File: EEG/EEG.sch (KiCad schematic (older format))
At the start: 45 parts, among them J1 USB_B_Micro, J2 Conn_01x08_Female, J3 Conn_01x08_Female, Q1 2N2219, Q2 2N2219, SW1 SW_Push, SW2 SW_Push, U1 AMS1117-3.3, U2 FT231XS, U3 ESP32-PICO-D4, U4 MAX7219

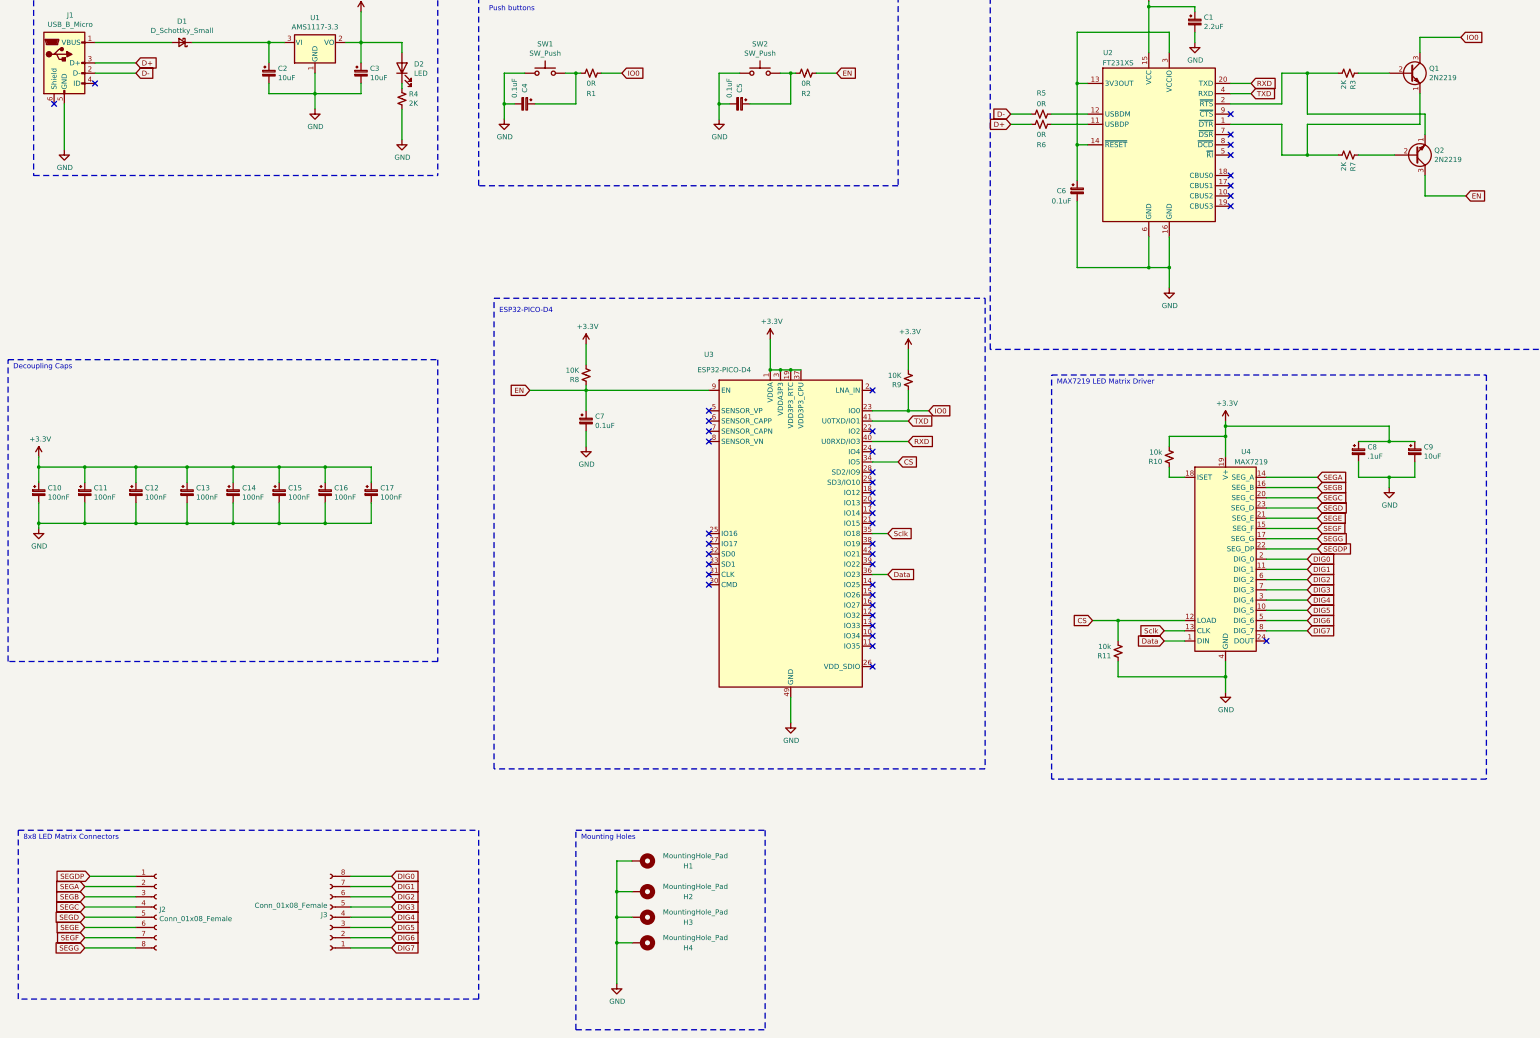
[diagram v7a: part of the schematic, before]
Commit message: added some pcb layout
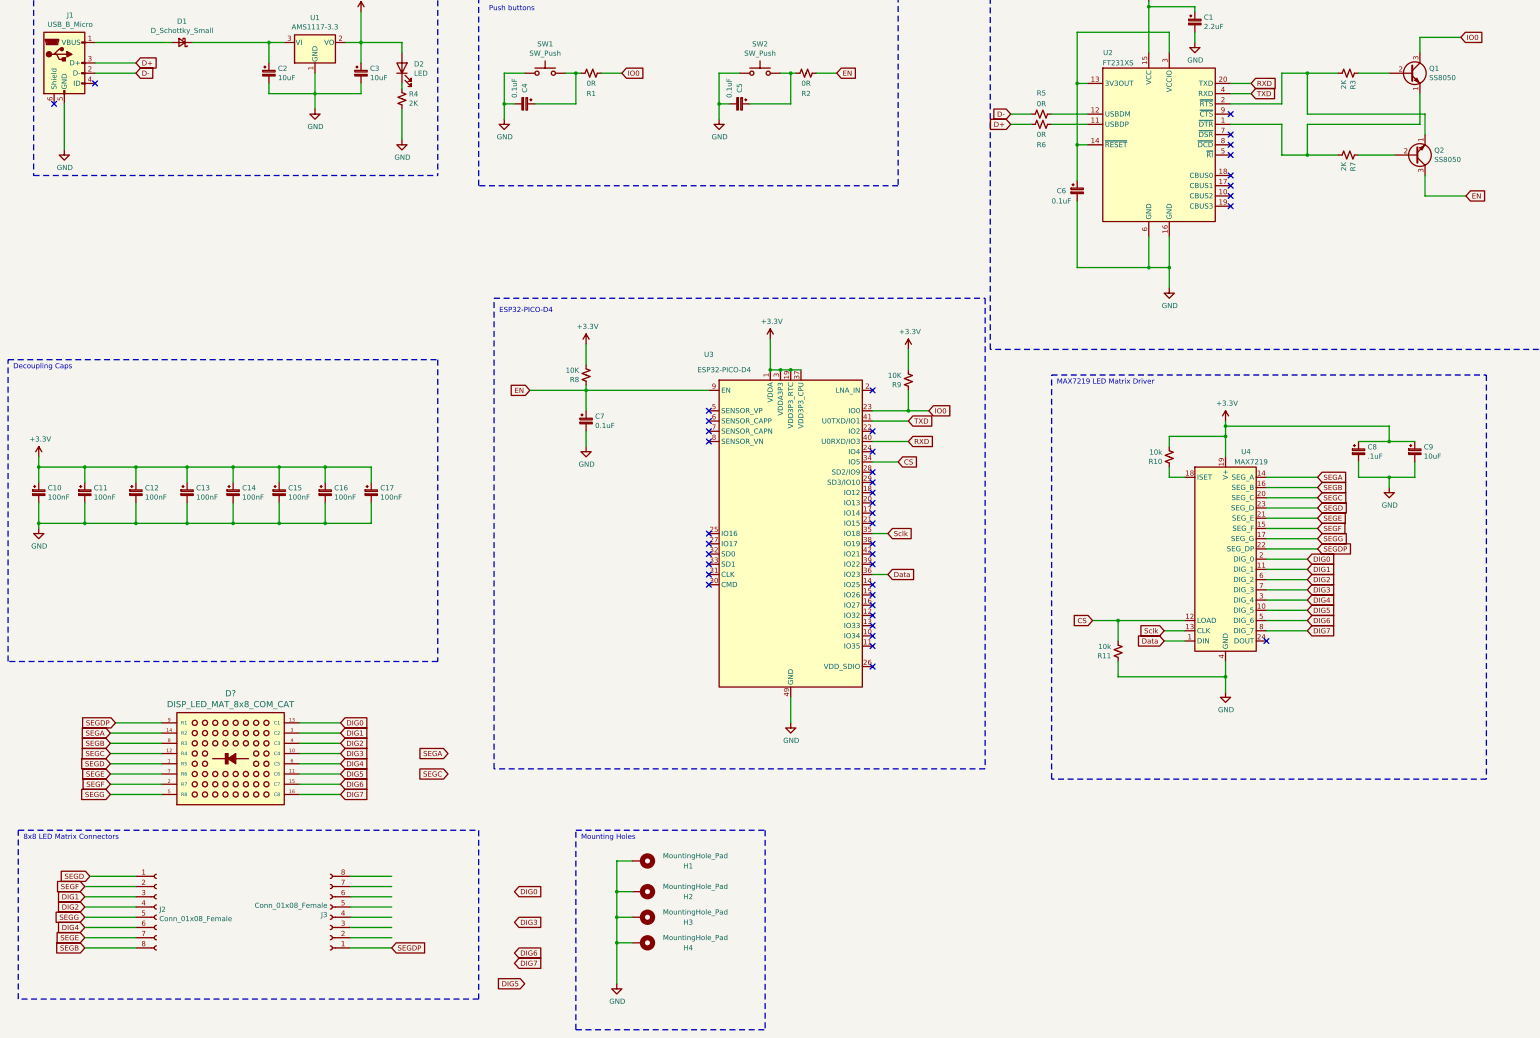
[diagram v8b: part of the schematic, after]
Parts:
- added D?: DISP_LED_MAT_8x8_COM_CAT, symbol akn_misc:DISP_LED_MAT_8x8_COM_CAT
- H1, H2, H3, H4: footprint (none) -> MountingHole:MountingHole_4.3mm_M4_Pad_Via
- Q1, Q2: value 2N2219 -> SS8050; footprint Package_TO_SOT_THT:TO-39-3 -> Package_TO_SOT_SMD:SOT-23
- U4: footprint MAX7219:DIL24 -> MAX7219:SOIC24
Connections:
- wire segments 199 -> 215
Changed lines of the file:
@@
 P 14450 1700
 F 0 "Q1" H 14640 1746 50  0000 L CNN
-F 1 "2N2219" H 14640 1655 50  0000 L CNN
-F 2 "Package_TO_SOT_THT:TO-39-3" H 14650 1625 50  0001 L CIN
+F 1 "SS8050" H 14640 1655 50  0000 L CNN
+F 2 "Package_TO_SOT_SMD:SOT-23" H 14650 1625 50  0001 L CIN
 F 3 "http://www.onsemi.com/pub_link/Collateral/2N2219-D.PDF" H 14450 1700 50  0001 L CNN
 	1    14450 1700
@@
 P 14500 2500
 F 0 "Q2" H 14690 2454 50  0000 L CNN
-F 1 "2N2219" H 14690 2545 50  0000 L CNN
-F 2 "Package_TO_SOT_THT:TO-39-3" H 14700 2425 50  0001 L CIN
+F 1 "SS8050" H 14690 2545 50  0000 L CNN
+F 2 "Package_TO_SOT_SMD:SOT-23" H 14700 2425 50  0001 L CIN
 F 3 "http://www.onsemi.com/pub_link/Collateral/2N2219-D.PDF" H 14500 2500 50  0001 L CNN
 	1    14500 2500
@@
 F 0 "U4" H 12850 7500 50  0000 C CNN
 F 1 "MAX7219" H 12900 7400 50  0000 C CNN
-F 2 "MAX7219:DIL24" H 12600 6500 50  0001 C CNN
+F 2 "MAX7219:SOIC24" H 12600 6500 50  0001 C CNN
 F 3 "https://datasheets.maximintegrated.com/en/ds/MAX7219-MAX7221.pdf" H 12700 6300 50  0001 C CNN
 	1    12650 6450
@@
 	1    0    0    -1
 $EndComp
-Text GLabel 1500 9650 0    50   Input ~ 0
-SEGA
-Text GLabel 1500 9750 0    50   Input ~ 0
-SEGB
-Text GLabel 1500 9850 0    50   Input ~ 0
-SEGC
-Text GLabel 1500 9950 0    50   Input ~ 0
-SEGD
-Text GLabel 1500 10050 0    50   Input ~ 0
-SEGE
-Text GLabel 1500 10150 0    50   Input ~ 0
-SEGF
-Text GLabel 1500 10250 0    50   Input ~ 0
-SEGG
-Text GLabel 1550 9550 0    50   Input ~ 0
-SEGDP
-Wire Wire Line
-	1500 9650 2000 9650
-Wire Wire Line
-	1500 9750 2000 9750
-Wire Wire Line
-	1500 9850 2000 9850
-Wire Wire Line
-	1500 9950 2000 9950
-Wire Wire Line
-	1500 10050 2000 10050
-Wire Wire Line
-	1500 10150 2000 10150
-Wire Wire Line
-	1500 10250 2000 10250
-Wire Wire Line
-	1550 9550 2000 9550
-Text GLabel 4500 9650 2    50   Input ~ 0
-DIG1
-Text GLabel 4500 9750 2    50   Input ~ 0
-DIG2
-Text GLabel 4500 9850 2    50   Input ~ 0
-DIG3
-Text GLabel 4500 9950 2    50   Input ~ 0
-DIG4
-Text GLabel 4500 10050 2    50   Input ~ 0
-DIG5
-Text GLabel 4500 10150 2    50   Input ~ 0
-DIG6
-Text GLabel 4500 9550 2    50   Input ~ 0
-DIG0
-Text GLabel 4500 10250 2    50   Input ~ 0
-DIG7
-Wire Wire Line
-	4100 9550 4500 9550
-Wire Wire Line
-	4100 9650 4500 9650
-Wire Wire Line
-	4100 9750 4500 9750
-Wire Wire Line
-	4100 9850 4500 9850
-Wire Wire Line
-	4100 9950 4500 9950
-Wire Wire Line
-	4100 10050 4500 10050
-Wire Wire Line
-	4100 10150 4500 10150
-Wire Wire Line
-	4100 10250 4500 10250
 Wire Wire Line
 	2550 1400 3300 1400
@@
 F 0 "H1" V 7000 9800 50  0000 L CNN
 F 1 "MountingHole_Pad" V 6900 9600 50  0000 L CNN
-F 2 "" H 6950 9400 50  0001 C CNN
+F 2 "MountingHole:MountingHole_4.3mm_M4_Pad_Via" H 6950 9400 50  0001 C CNN
 F 3 "~" H 6950 9400 50  0001 C CNN
 	1    6950 9400
@@
 F 0 "H2" V 7000 10100 50  0000 L CNN
 F 1 "MountingHole_Pad" V 6900 9900 50  0000 L CNN
-F 2 "" H 6950 9700 50  0001 C CNN
+F 2 "MountingHole:MountingHole_4.3mm_M4_Pad_Via" H 6950 9700 50  0001 C CNN
 F 3 "~" H 6950 9700 50  0001 C CNN
 	1    6950 9700
@@
 F 0 "H3" V 7000 10350 50  0000 L CNN
 F 1 "MountingHole_Pad" V 6900 10150 50  0000 L CNN
-F 2 "" H 6950 9950 50  0001 C CNN
+F 2 "MountingHole:MountingHole_4.3mm_M4_Pad_Via" H 6950 9950 50  0001 C CNN
 F 3 "~" H 6950 9950 50  0001 C CNN
 	1    6950 9950
@@
 F 0 "H4" V 7000 10600 50  0000 L CNN
 F 1 "MountingHole_Pad" V 6900 10400 50  0000 L CNN
-F 2 "" H 6950 10200 50  0001 C CNN
+F 2 "MountingHole:MountingHole_4.3mm_M4_Pad_Via" H 6950 10200 50  0001 C CNN
 F 3 "~" H 6950 10200 50  0001 C CNN
 	1    6950 10200
@@
 	1    0    0    -1
 $EndComp
+Text GLabel 1750 8150 0    50   Input ~ 0
+SEGA
+Text GLabel 1750 8250 0    50   Input ~ 0
+SEGB
+Text GLabel 1750 8350 0    50   Input ~ 0
+SEGC
+Text GLabel 1750 8450 0    50   Input ~ 0
+SEGD
+Text GLabel 1750 8550 0    50   Input ~ 0
+SEGE
+Text GLabel 1750 8650 0    50   Input ~ 0
+SEGF
+Text GLabel 1750 8750 0    50   Input ~ 0
+SEGG
+Wire Wire Line
+	1750 8150 2250 8150
+Wire Wire Line
+	1750 8250 2250 8250
+Wire Wire Line
+	1750 8350 2250 8350
+Wire Wire Line
+	1750 8450 2250 8450
+Wire Wire Line
+	1750 8550 2250 8550
+Wire Wire Line
+	1750 8650 2250 8650
+Wire Wire Line
+	1750 8750 2250 8750
+Text GLabel 4000 8150 2    50   Input ~ 0
+DIG1
+Text GLabel 4000 8250 2    50   Input ~ 0
+DIG2
+Text GLabel 4000 8350 2    50   Input ~ 0
+DIG3
+Text GLabel 4000 8450 2    50   Input ~ 0
+DIG4
+Text GLabel 4000 8550 2    50   Input ~ 0
+DIG5
+Text GLabel 4000 8650 2    50   Input ~ 0
+DIG6
+Text GLabel 4000 8050 2    50   Input ~ 0
+DIG0
+Text GLabel 4000 8750 2    50   Input ~ 0
+DIG7
+Wire Wire Line
+	3600 8050 4000 8050
+Wire Wire Line
+	3600 8150 4000 8150
+Wire Wire Line
+	3600 8250 4000 8250
+Wire Wire Line
+	3600 8350 4000 8350
+Wire Wire Line
+	3600 8450 4000 8450
+Wire Wire Line
+	3600 8550 4000 8550
+Wire Wire Line
+	3600 8650 4000 8650
+Wire Wire Line
+	3600 8750 4000 8750
+Wire Wire Line
+	4100 10250 4500 10250
+Wire Wire Line
+	4100 10150 4500 10150
+Wire Wire Line
+	4100 10050 4500 10050
+Wire Wire Line
+	4100 9950 4500 9950
+Wire Wire Line
+	4100 9850 4500 9850
+Wire Wire Line
+	4100 9750 4500 9750
+Wire Wire Line
+	4100 9650 4500 9650
+Wire Wire Line
+	4100 9550 4500 9550
+Text GLabel 5700 10400 2    50   Input ~ 0
+DIG7
+Text GLabel 5700 9700 2    50   Input ~ 0
+DIG0
+Text GLabel 5700 10300 2    50   Input ~ 0
+DIG6
+Text GLabel 5800 10600 0    50   Input ~ 0
+DIG5
+Text GLabel 1500 10050 0    50   Input ~ 0
+DIG4
+Text GLabel 5700 10000 2    50   Input ~ 0
+DIG3
+Text GLabel 1500 9850 0    50   Input ~ 0
+DIG2
+Text GLabel 1500 9750 0    50   Input ~ 0
+DIG1
+Wire Wire Line
+	1550 9550 2000 9550
+Wire Wire Line
+	1500 10250 2000 10250
+Wire Wire Line
+	1500 10150 2000 10150
+Wire Wire Line
+	1500 10050 2000 10050
+Wire Wire Line
+	1500 9950 2000 9950
+Wire Wire Line
+	1500 9850 2000 9850
+Wire Wire Line
+	1500 9750 2000 9750
+Wire Wire Line
+	1500 9650 2000 9650
+Text GLabel 4500 10250 2    50   Input ~ 0
+SEGDP
+Text GLabel 1500 9950 0    50   Input ~ 0
+SEGG
+Text GLabel 1500 9650 0    50   Input ~ 0
+SEGF
+Text GLabel 1500 10150 0    50   Input ~ 0
+SEGE
+Text GLabel 1550 9550 0    50   Input ~ 0
+SEGD
+Text GLabel 5050 8550 0    50   Input ~ 0
+SEGC
+Text GLabel 1500 10250 0    50   Input ~ 0
+SEGB
+Text GLabel 5050 8350 0    50   Input ~ 0
+SEGA
+Text GLabel 1800 8050 0    50   Input ~ 0
+SEGDP
+$Comp
+L akn_misc:DISP_LED_MAT_8x8_COM_CAT D?
+U 1 1 60652E1D
+P 2250 8850
+F 0 "D?" H 2925 9937 60  0000 C CNN
+F 1 "DISP_LED_MAT_8x8_COM_CAT" H 2925 9831 60  0000 C CNN
+F 2 "" H 2350 8800 60  0000 C CNN
+F 3 "" H 2350 8800 60  0000 C CNN
+	1    2250 8850
+	1    0    0    -1
+$EndComp
+Wire Wire Line
+	1800 8050 2250 8050
 $EndSCHEMATC
